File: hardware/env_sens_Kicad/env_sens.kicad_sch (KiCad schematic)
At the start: 40 parts, among them J1 CO2_Conn, J2 BATTERY, J3 USB_C_Receptacle_USB2.0_14P, J4 CAN_BUS, SW1 RESET, SW2 BOOT, U1 HDC1080, U2 TCAN1043xDxQ1, U3 ESP32-S3-WROOM-1, U6 TPD1E05U06DYA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

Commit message: Added central power source configuration from mother board
Central power source configuration from mother board + safety regulation
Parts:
- added D3, D4: D, symbol Device:D
- added J5: Conn_01x02_Pin, Connector_PinHeader_2.00mm:PinHeader_1x02_P2.00mm_Vertical_SMD_Pin1Right, symbol Connector:Conn_01x02_Pin
- H1, H2, H3, H4: footprint MountingHole:MountingHole_3.2mm_M3_DIN965_Pad_TopBottom -> MountingHole:MountingHole_2.7mm_M2.5
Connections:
- net +3V3: now also D3.1 (K), D4.1 (K); no longer 3V3_Reg1.2 (VO), C4.1, R7.1
- net GND: now also J5.2 (Pin_2)
- new net +3.3V: 3V3_Reg1.2 (VO), C4.1, D3.2 (A), R7.1
- new net +3.3VA: D4.2 (A), J5.1 (Pin_1)
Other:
- note added: "5V -> 3.3V"
- note added: "5V regulator"
- note added: "CAN Transceiver"
- note added: "CHANGE TRANSCEIVER FROM 5V TO 3.3V SOME EXAMPLES I FOUND WITH CHATGPT: MCP2562FD SN65HVD230 TJA1051T/3"
- note added: "Central Power Source Configuration Safety Regulation"
- note added: "ESP32 MCU"
- note added: "Humidity + Temperature Sensor"
- note added: "Mounting Holes"
- note added: "Type C"
- moved on the sheet: 3V3_Reg1, 5V_Reg1, C1, C10, C11, C2, C3, C4, C5, C6, C7, C8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

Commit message: Changed MB input voltage to 5V
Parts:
- removed C11: 4.7n, Capacitor_SMD:C_0603_1608Metric_Pad1.08x0.95mm_HandSolder, symbol Device:C
- removed R5, R6: 60, Resistor_SMD:R_0603_1608Metric_Pad0.98x0.95mm_HandSolder, symbol Device:R
- added D5: D, symbol Device:D
- added J6: CAN_BUS_in, Connector_JST:JST_EH_S2B-EH_1x02_P2.50mm_Horizontal, symbol Connector:Conn_01x02_Socket
- J4: value CAN_BUS -> CAN_BUS_out; footprint Connector_JST:JST_PH_S2B-PH-SM4-TB_1x02-1MP_P2.00mm_Horizontal -> Connector_JST:JST_EH_S2B-EH_1x02_P2.50mm_Horizontal
- J5: footprint Connector_PinHeader_2.00mm:PinHeader_1x02_P2.00mm_Vertical_SMD_Pin1Right -> Connector_JST:JST_EH_S2B-EH_1x02_P2.50mm_Horizontal
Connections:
- net +3.3V: no longer D3.2 (A)
- net +3V3: no longer D3.1 (K), D4.1 (K)
- net +5V: now also D3.1 (K), D4.1 (K), D5.1 (K); no longer 5V_Reg1.2 (VO), C1.1, J3.A4 (VBUS), J3.A9 (VBUS), J3.B4 (VBUS), J3.B9 (VBUS), U6.2 (GND)
- net CANH: now also J6.2 (Pin_2)
- net CANL: now also J6.1 (Pin_1)
- net +3.3VA renamed +5V_mb
- new net +5V_reg: 5V_Reg1.2 (VO), C1.1, D3.2 (A)
- new net +5V_usb: D5.2 (A), J3.A4 (VBUS), J3.A9 (VBUS), J3.B4 (VBUS), J3.B9 (VBUS), U6.2 (GND)
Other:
- note added: "CO2 Sensor"

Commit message: Updated layout with schematic changes
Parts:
- D3, D4, D5: footprint (none) -> Diode_SMD:D_SOD-123F
- J2: footprint Connector_AMASS:AMASS_XT60PW-M_1x02_P7.20mm_Horizontal -> Connector_AMASS:AMASS_XT30PW-M_1x02_P2.50mm_Horizontal
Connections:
- net +3.3V is gone; now on net +3V3: 3V3_Reg1.2 (VO), C4.1, R7.1
- net CANH: now also J4.1 (Pin_1), J6.1 (Pin_1); no longer J4.2 (Pin_2), J6.2 (Pin_2)
- net CANL: now also J4.2 (Pin_2), J6.2 (Pin_2); no longer J4.1 (Pin_1), J6.1 (Pin_1)
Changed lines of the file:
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@@
 	)
 	(junction
+		(at 248.92 133.35)
+		(diameter 0)
+		(color 0 0 0 0)
+	)
+	(junction
 		(at 148.59 74.93)
 		(diameter 0)
@@
 	)
 	(junction
-		(at 255.27 133.35)
+		(at 77.47 100.33)
 		(diameter 0)
 		(color 0 0 0 0)
 	)
 	(junction
-		(at 77.47 100.33)
+		(at 243.84 133.35)
 		(diameter 0)
 		(color 0 0 0 0)
 	)
 	(junction
-		(at 243.84 133.35)
+		(at 255.27 135.89)
 		(diameter 0)
 		(color 0 0 0 0)
@@
 	)
 	(junction
-		(at 256.54 137.16)
-		(diameter 0)
-		(color 0 0 0 0)
-	)
-	(junction
 		(at 261.62 27.94)
 		(diameter 0)
@@
 	(wire
 		(pts
-			(xy 259.08 135.89) (xy 259.08 137.16)
-		)
-		(stroke
-			(width 0)
-			(type default)
-		)
-	)
-	(wire
-		(pts
 			(xy 92.71 127) (xy 107.95 127)
 		)
@@
 	(wire
 		(pts
-			(xy 248.92 133.35) (xy 248.92 137.16)
-		)
-		(stroke
-			(width 0)
-			(type default)
-		)
-	)
-	(wire
-		(pts
 			(xy 232.41 62.23) (xy 247.65 62.23)
 		)
@@
 	(wire
 		(pts
-			(xy 259.08 133.35) (xy 255.27 133.35)
-		)
-		(stroke
-			(width 0)
-			(type default)
-		)
-	)
-	(wire
-		(pts
 			(xy 83.82 100.33) (xy 93.98 100.33)
 		)
@@
 	(wire
 		(pts
-			(xy 256.54 128.27) (xy 256.54 137.16)
+			(xy 45.72 109.22) (xy 48.26 109.22)
 		)
 		(stroke
@@
 	(wire
 		(pts
-			(xy 45.72 109.22) (xy 48.26 109.22)
+			(xy 35.56 116.84) (xy 48.26 116.84)
 		)
 		(stroke
@@
 	(wire
 		(pts
-			(xy 35.56 116.84) (xy 48.26 116.84)
+			(xy 196.85 102.87) (xy 196.85 105.41)
 		)
 		(stroke
@@
 	(wire
 		(pts
-			(xy 196.85 102.87) (xy 196.85 105.41)
+			(xy 261.62 27.94) (xy 267.97 27.94)
 		)
 		(stroke
@@
 	(wire
 		(pts
-			(xy 261.62 27.94) (xy 267.97 27.94)
+			(xy 218.44 69.85) (xy 218.44 73.66)
 		)
 		(stroke
@@
 	(wire
 		(pts
-			(xy 218.44 69.85) (xy 218.44 73.66)
+			(xy 248.92 133.35) (xy 259.08 133.35)
 		)
 		(stroke
@@
 	(wire
 		(pts
-			(xy 77.47 100.33) (xy 77.47 111.76)
+			(xy 255.27 128.27) (xy 255.27 135.89)
 		)
 		(stroke
@@
 	(wire
 		(pts
-			(xy 243.84 133.35) (xy 248.92 133.35)
+			(xy 77.47 100.33) (xy 77.47 111.76)
 		)
 		(stroke
@@
 	(wire
 		(pts
-			(xy 255.27 133.35) (xy 255.27 135.89)
+			(xy 243.84 133.35) (xy 248.92 133.35)
 		)
 		(stroke
@@
 	(wire
 		(pts
-			(xy 259.08 125.73) (xy 255.27 125.73)
+			(xy 92.71 142.24) (xy 101.6 142.24)
 		)
 		(stroke
@@
 	(wire
 		(pts
-			(xy 92.71 142.24) (xy 101.6 142.24)
+			(xy 246.38 40.64) (xy 261.62 40.64)
 		)
 		(stroke
@@
 	(wire
 		(pts
-			(xy 246.38 40.64) (xy 261.62 40.64)
+			(xy 209.55 133.35) (xy 243.84 133.35)
 		)
 		(stroke
@@
 	(wire
 		(pts
-			(xy 209.55 133.35) (xy 243.84 133.35)
+			(xy 229.87 59.69) (xy 245.11 59.69)
 		)
 		(stroke
@@
 	(wire
 		(pts
-			(xy 229.87 59.69) (xy 245.11 59.69)
+			(xy 248.92 125.73) (xy 248.92 133.35)
 		)
 		(stroke
@@
 	(wire
 		(pts
-			(xy 255.27 125.73) (xy 255.27 133.35)
+			(xy 255.27 135.89) (xy 259.08 135.89)
 		)
 		(stroke
@@
 	(wire
 		(pts
+			(xy 248.92 125.73) (xy 259.08 125.73)
+		)
+		(stroke
+			(width 0)
+			(type default)
+		)
+	)
+	(wire
+		(pts
 			(xy 83.82 107.95) (xy 93.98 107.95)
 		)
@@
 	(wire
 		(pts
-			(xy 259.08 128.27) (xy 256.54 128.27)
+			(xy 259.08 128.27) (xy 255.27 128.27)
 		)
 		(stroke
@@
 	(wire
 		(pts
-			(xy 256.54 137.16) (xy 248.92 137.16)
-		)
-		(stroke
-			(width 0)
-			(type default)
-		)
-	)
-	(wire
-		(pts
-			(xy 259.08 137.16) (xy 256.54 137.16)
-		)
-		(stroke
-			(width 0)
-			(type default)
-		)
-	)
-	(wire
-		(pts
 			(xy 247.65 62.23) (xy 247.65 74.93)
 		)
@@
 			)
 		)
-		(property "Footprint" ""
+		(property "Footprint" "Diode_SMD:D_SOD-123F"
 			(at 140.97 160.02 0)
 			(effects
@@
 			)
 		)
-		(property "Footprint" ""
+		(property "Footprint" "Diode_SMD:D_SOD-123F"
 			(at 147.32 163.83 0)
 			(effects
@@
 			)
 		)
-		(property "Footprint" "Connector_AMASS:AMASS_XT60PW-M_1x02_P7.20mm_Horizontal"
+		(property "Footprint" "Connector_AMASS:AMASS_XT30PW-M_1x02_P2.50mm_Horizontal"
 			(at 43.18 63.5 0)
 			(effects
@@
 			)
 		)
-		(property "Value" "+3.3V"
+		(property "Value" "+3V3"
 			(at 157.48 27.94 0)
 			(effects
@@
 			)
 		)
-		(property "Footprint" ""
+		(property "Footprint" "Diode_SMD:D_SOD-123F"
 			(at 134.62 163.83 0)
 			(effects

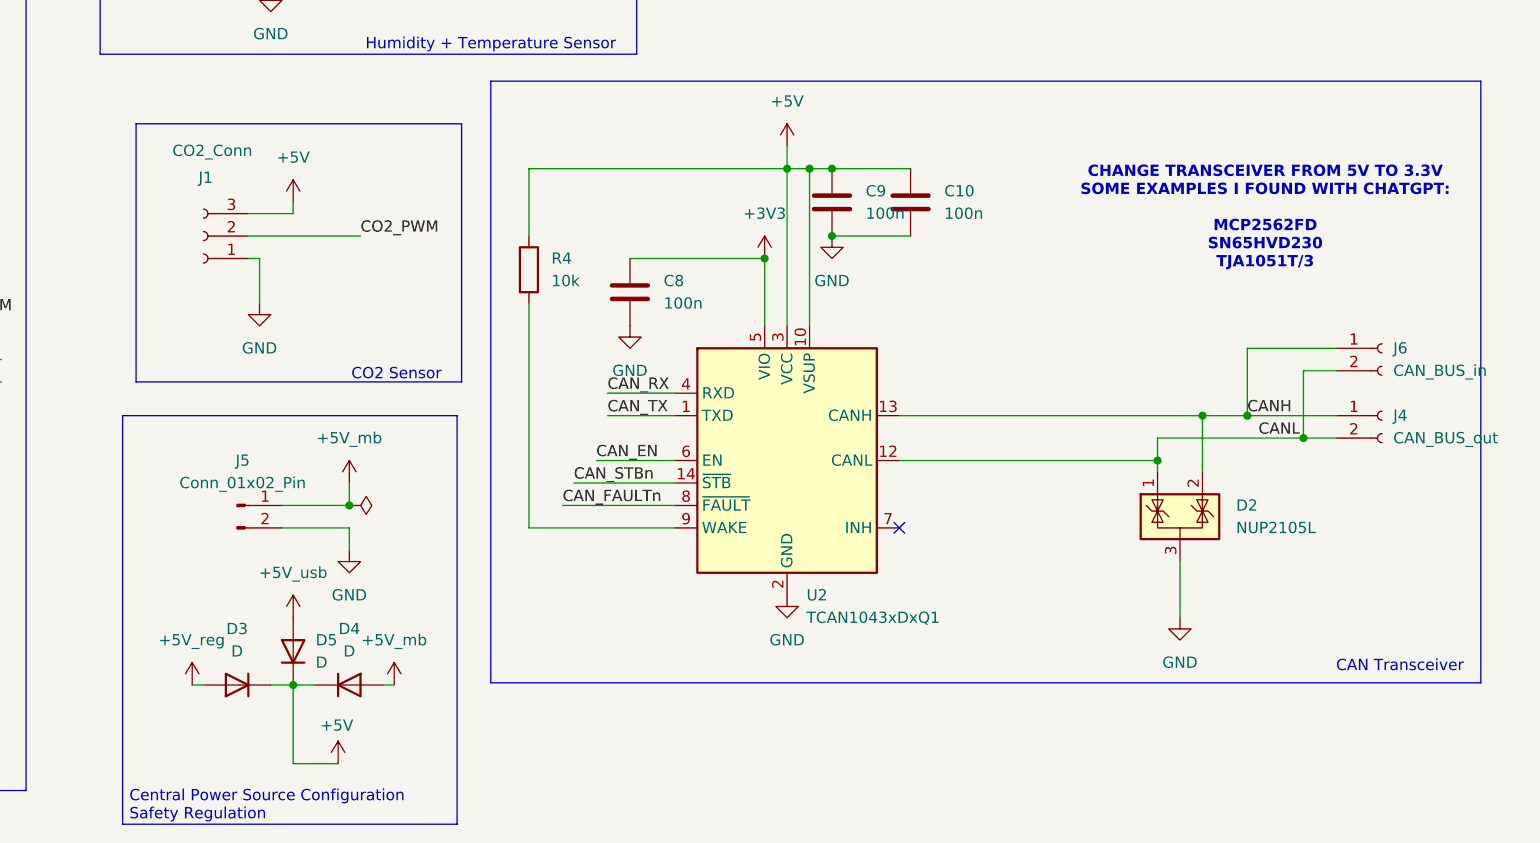
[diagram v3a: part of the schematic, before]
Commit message: Replaced with schottkey dioides & did production files
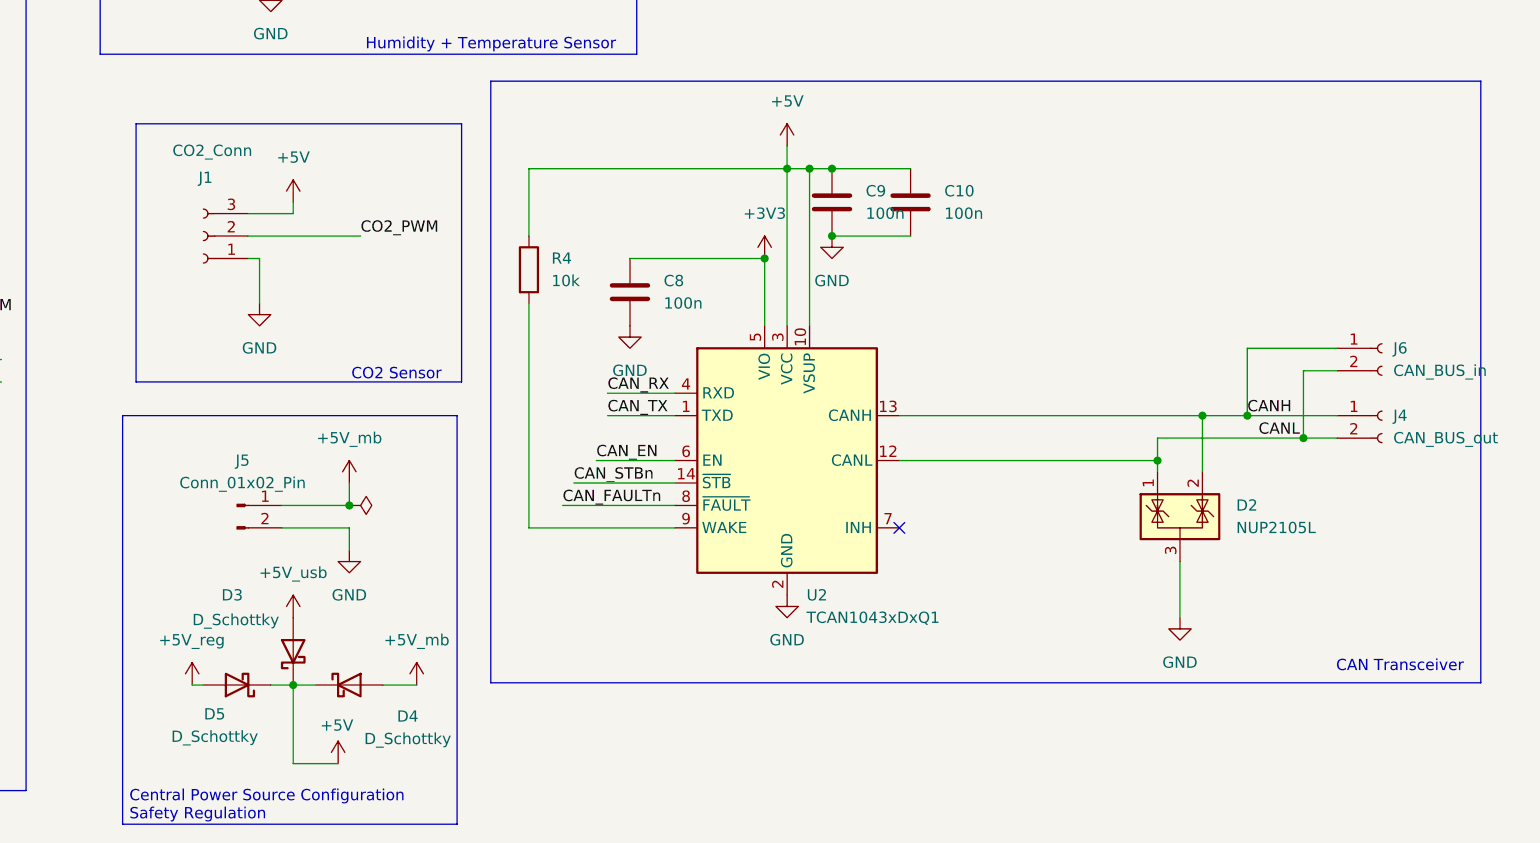
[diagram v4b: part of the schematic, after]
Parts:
- removed D3, D4, D5: D, Diode_SMD:D_SOD-123F, symbol Device:D
- added D3, D4, D5: D_Schottky, Diode_SMD:D_SOD-123, symbol Device:D_Schottky
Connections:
- net +5V: now also D3.1 (K), D4.1 (K), D5.1 (K)
- net +5V_mb: now also D4.2 (A)
- net +5V_reg: now also D5.2 (A)
- net +5V_usb: now also D3.2 (A)
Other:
- note removed: "CHANGE TRANSCEIVER FROM 5V TO 3.3V SOME EXAMPLES I FOUND WITH CHATGPT: MCP2562FD SN65HVD230 TJA1051T/3"
